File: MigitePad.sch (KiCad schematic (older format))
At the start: 74 parts, among them J1 OLED, J2 LED-Lily58-cache, SW1 SW_Push, SW2 Rotary_Encoder_Switch, U1 ProMicro

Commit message: Rewired Encoder
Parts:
- added H9: MountingHole, Lily58-footprint:HOLE_M2_TH, symbol Mechanical:MountingHole
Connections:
- net COL3: now also SW2.S2
- net COL6: no longer SW2.S2
- net ROW0: now also D31.1 (K)
- net ROW1: no longer D31.1 (K)
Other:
- moved on the sheet: D31, SW2
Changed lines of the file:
@@
 	8250 2800 8250 3750
 Wire Wire Line
-	6900 2000 6900 1600
+	6900 2000 6900 1650
 Wire Wire Line
 	7350 2000 7350 1600
 Wire Wire Line
 	7800 2000 7800 1600
-Wire Wire Line
-	8250 2000 8250 1750
 Wire Wire Line
 	5700 2400 6650 2400
@@
 L Device:Rotary_Encoder_Switch SW2
 U 1 1 5E65AE52
-P 9000 2100
-F 0 "SW2" H 9000 2467 50  0000 C CNN
-F 1 "Rotary_Encoder_Switch" H 9000 2376 50  0000 C CNN
-F 2 "Keebio-Parts:RotaryEncoder_EC11" H 8850 2260 50  0001 C CNN
-F 3 "~" H 9000 2360 50  0001 C CNN
-	1    9000 2100
+P 6950 1000
+F 0 "SW2" H 6950 1367 50  0000 C CNN
+F 1 "Rotary_Encoder_Switch" H 6950 1276 50  0000 C CNN
+F 2 "Keebio-Parts:RotaryEncoder_EC11" H 6800 1160 50  0001 C CNN
+F 3 "~" H 6950 1260 50  0001 C CNN
+	1    6950 1000
 	-1   0    0    1
 $EndComp
@@
 L Device:D_Small D31
 U 1 1 5E668E53
-P 8700 2300
-F 0 "D31" V 8746 2232 50  0000 R CNN
-F 1 "D_Small" V 8655 2232 50  0000 R CNN
-F 2 "Lily58-footprint:Diode_TH_SOD123" V 8700 2300 50  0001 C CNN
-F 3 "~" V 8700 2300 50  0001 C CNN
-	1    8700 2300
+P 6650 1200
+F 0 "D31" V 6696 1132 50  0000 R CNN
+F 1 "D_Small" V 6605 1132 50  0000 R CNN
+F 2 "Lily58-footprint:Diode_TH_SOD123" V 6650 1200 50  0001 C CNN
+F 3 "~" V 6650 1200 50  0001 C CNN
+	1    6650 1200
 	0    -1   -1   0
 $EndComp
-Wire Wire Line
-	8000 2400 8700 2400
-Connection ~ 8000 2400
-Wire Wire Line
-	8700 2000 8700 1750
-Wire Wire Line
-	8700 1750 8250 1750
-Connection ~ 8250 1750
-Wire Wire Line
-	8250 1750 8250 1600
 Text GLabel 1500 950  0    50   Input ~ 0
 RETX
 Text GLabel 1500 1050 0    50   Input ~ 0
 RERX
-Text GLabel 9300 2000 2    50   Input ~ 0
+Text GLabel 7250 900  2    50   Input ~ 0
 RETX
-Text GLabel 9300 2200 2    50   Input ~ 0
+Text GLabel 7250 1100 2    50   Input ~ 0
 RERX
 $Comp
 L power:GND #PWR0110
 U 1 1 5E68B0C4
-P 9650 2100
-F 0 "#PWR0110" H 9650 1850 50  0001 C CNN
-F 1 "GND" H 9655 1927 50  0000 C CNN
-F 2 "" H 9650 2100 50  0001 C CNN
-F 3 "" H 9650 2100 50  0001 C CNN
-	1    9650 2100
-	1    0    0    -1
-$EndComp
-Wire Wire Line
-	9300 2100 9650 2100
+P 7600 1000
+F 0 "#PWR0110" H 7600 750 50  0001 C CNN
+F 1 "GND" H 7605 827 50  0000 C CNN
+F 2 "" H 7600 1000 50  0001 C CNN
+F 3 "" H 7600 1000 50  0001 C CNN
+	1    7600 1000
+	1    0    0    -1
+$EndComp
+Wire Wire Line
+	7250 1000 7600 1000
+$Comp
+L Mechanical:MountingHole H9
+U 1 1 5E65D16B
+P 3350 7000
+F 0 "H9" H 3450 7046 50  0000 L CNN
+F 1 "MountingHole" H 3450 6955 50  0000 L CNN
+F 2 "Lily58-footprint:HOLE_M2_TH" H 3350 7000 50  0001 C CNN
+F 3 "~" H 3350 7000 50  0001 C CNN
+	1    3350 7000
+	1    0    0    -1
+$EndComp
+Wire Wire Line
+	8250 1600 8250 2000
+Wire Wire Line
+	5700 1750 6650 1750
+Wire Wire Line
+	6650 1750 6650 1300
+Connection ~ 5700 1750
+Wire Wire Line
+	6650 900  6450 900
+Wire Wire Line
+	6450 900  6450 1650
+Wire Wire Line
+	6450 1650 6900 1650
+Connection ~ 6900 1650
+Wire Wire Line
+	6900 1650 6900 1600
 $EndSCHEMATC

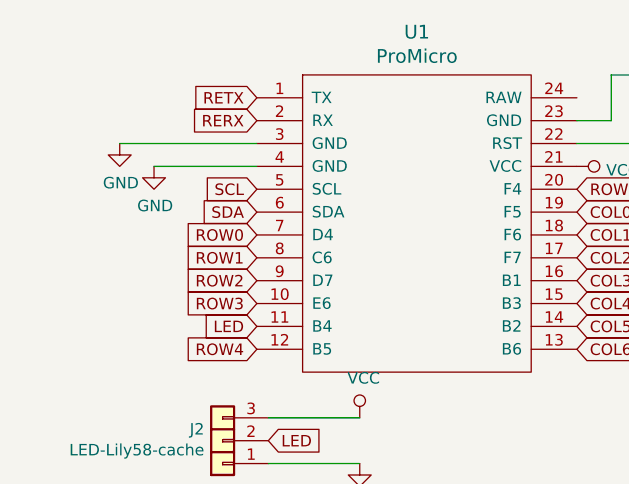
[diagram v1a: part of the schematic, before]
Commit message: Removed old Gerbers, fixed more traces
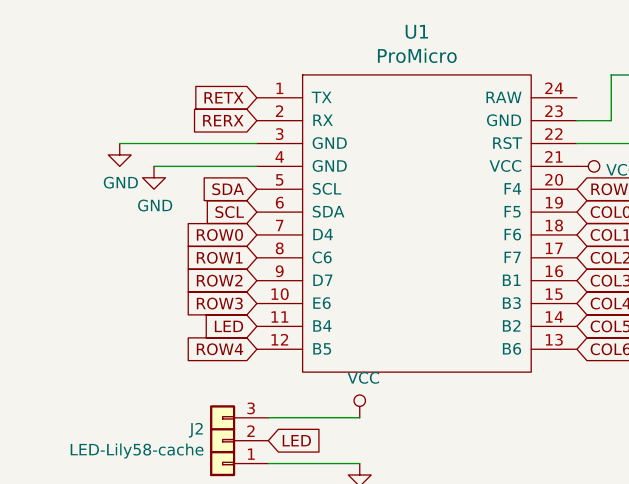
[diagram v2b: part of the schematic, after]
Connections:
- net SCL: now also U1.6 (SDA); no longer U1.5 (SCL)
- net SDA: now also U1.5 (SCL); no longer U1.6 (SDA)
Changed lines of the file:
@@
 Wire Wire Line
 	1550 2950 1750 2950
+Text GLabel 1500 1450 0    50   Input ~ 0
+SCL
 Text GLabel 1500 1350 0    50   Input ~ 0
-SCL
-Text GLabel 1500 1450 0    50   Input ~ 0
 SDA
 Text GLabel 1800 3150 2    50   Input ~ 0
